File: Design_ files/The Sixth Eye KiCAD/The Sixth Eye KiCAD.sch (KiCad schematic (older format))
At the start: 13 parts, among them J1 Battery conn, J2 US Sensor conn., J3 Vibration out, U1 ATmega328-AU, U2 LTC3525ISC6-5, Y1 8Mhz

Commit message: ploted
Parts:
- added R?: R, symbol Device:R
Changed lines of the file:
@@
 Wire Wire Line
 	4050 4850 4450 4850
+$Comp
+L Device:R R?
+U 1 1 6104FBF0
+P 8700 4950
+F 0 "R?" H 8770 4996 50  0000 L CNN
+F 1 "R" H 8770 4905 50  0000 L CNN
+F 2 "" V 8630 4950 50  0001 C CNN
+F 3 "~" H 8700 4950 50  0001 C CNN
+	1    8700 4950
+	1    0    0    -1
+$EndComp
 $EndSCHEMATC

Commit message: gerbers & drill files
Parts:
- removed R?: R, symbol Device:R
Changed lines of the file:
@@
 Wire Wire Line
 	4050 4850 4450 4850
-$Comp
-L Device:R R?
-U 1 1 6104FBF0
-P 8700 4950
-F 0 "R?" H 8770 4996 50  0000 L CNN
-F 1 "R" H 8770 4905 50  0000 L CNN
-F 2 "" V 8630 4950 50  0001 C CNN
-F 3 "~" H 8700 4950 50  0001 C CNN
-	1    8700 4950
-	1    0    0    -1
-$EndComp
 $EndSCHEMATC

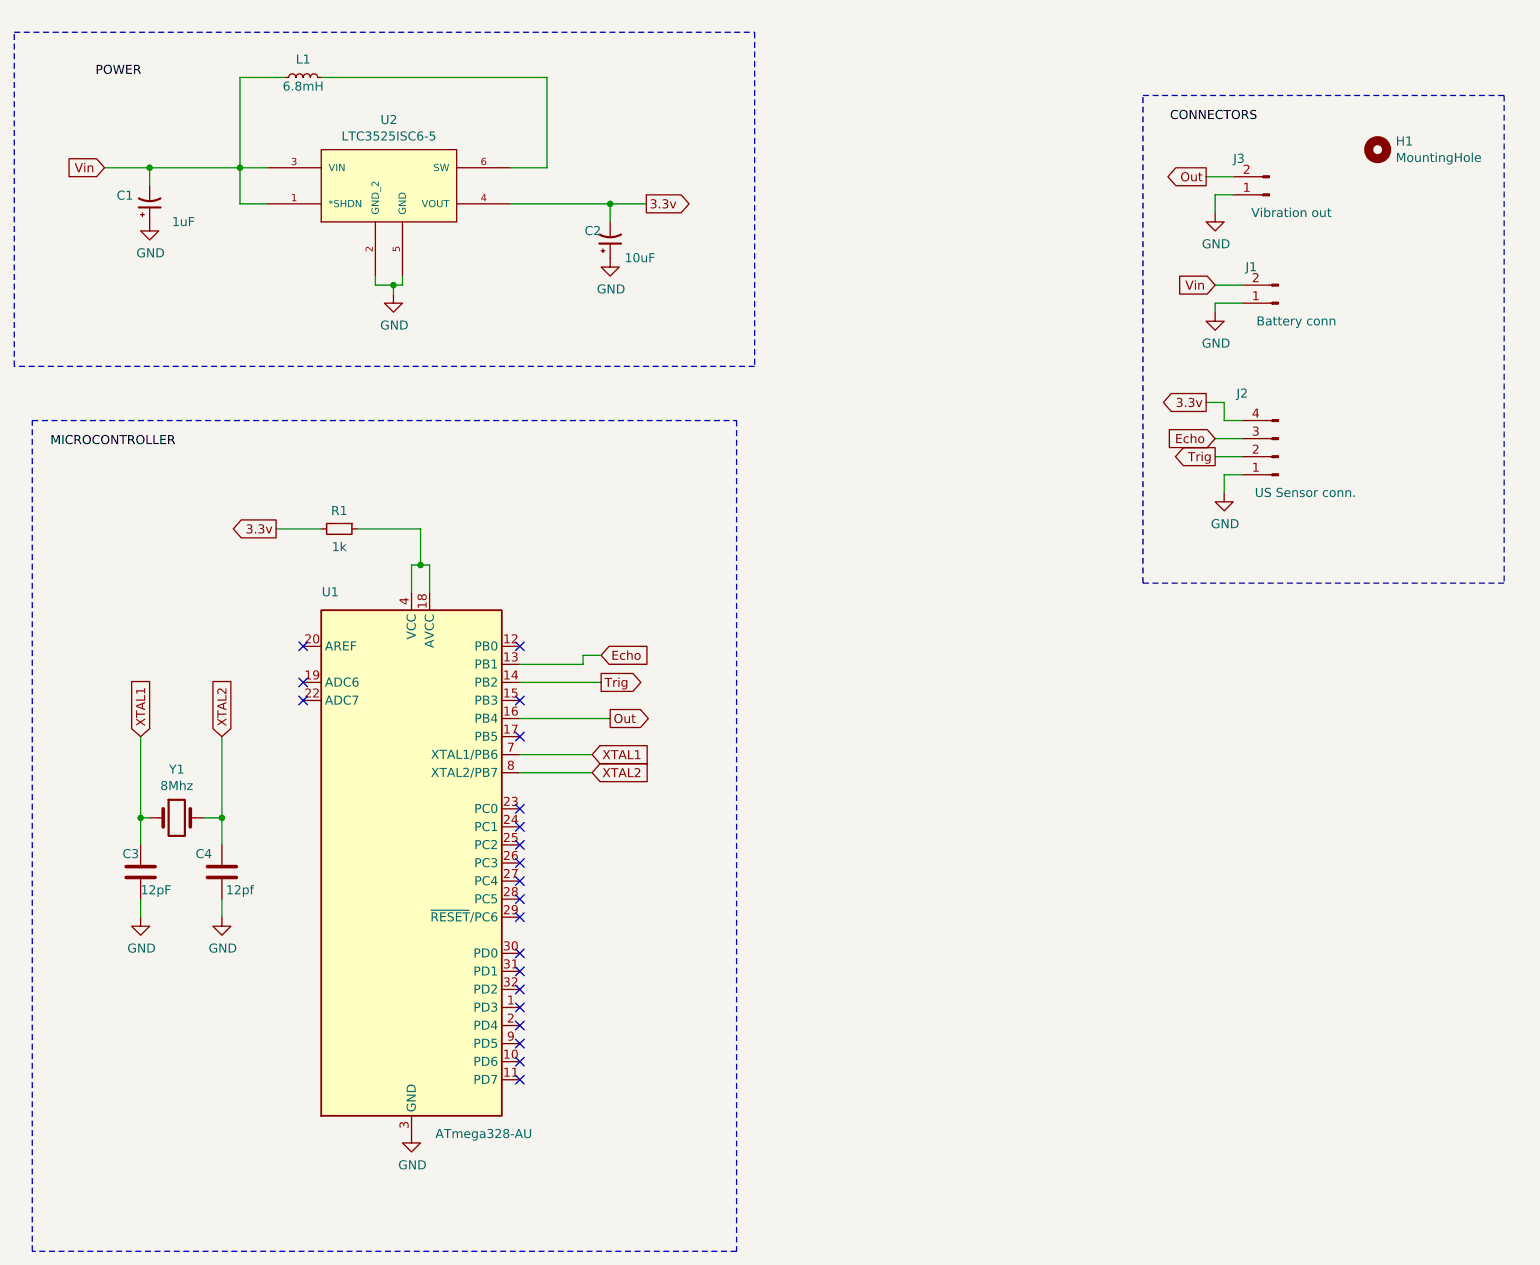
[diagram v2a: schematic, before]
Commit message: Accelerometer added to schematics
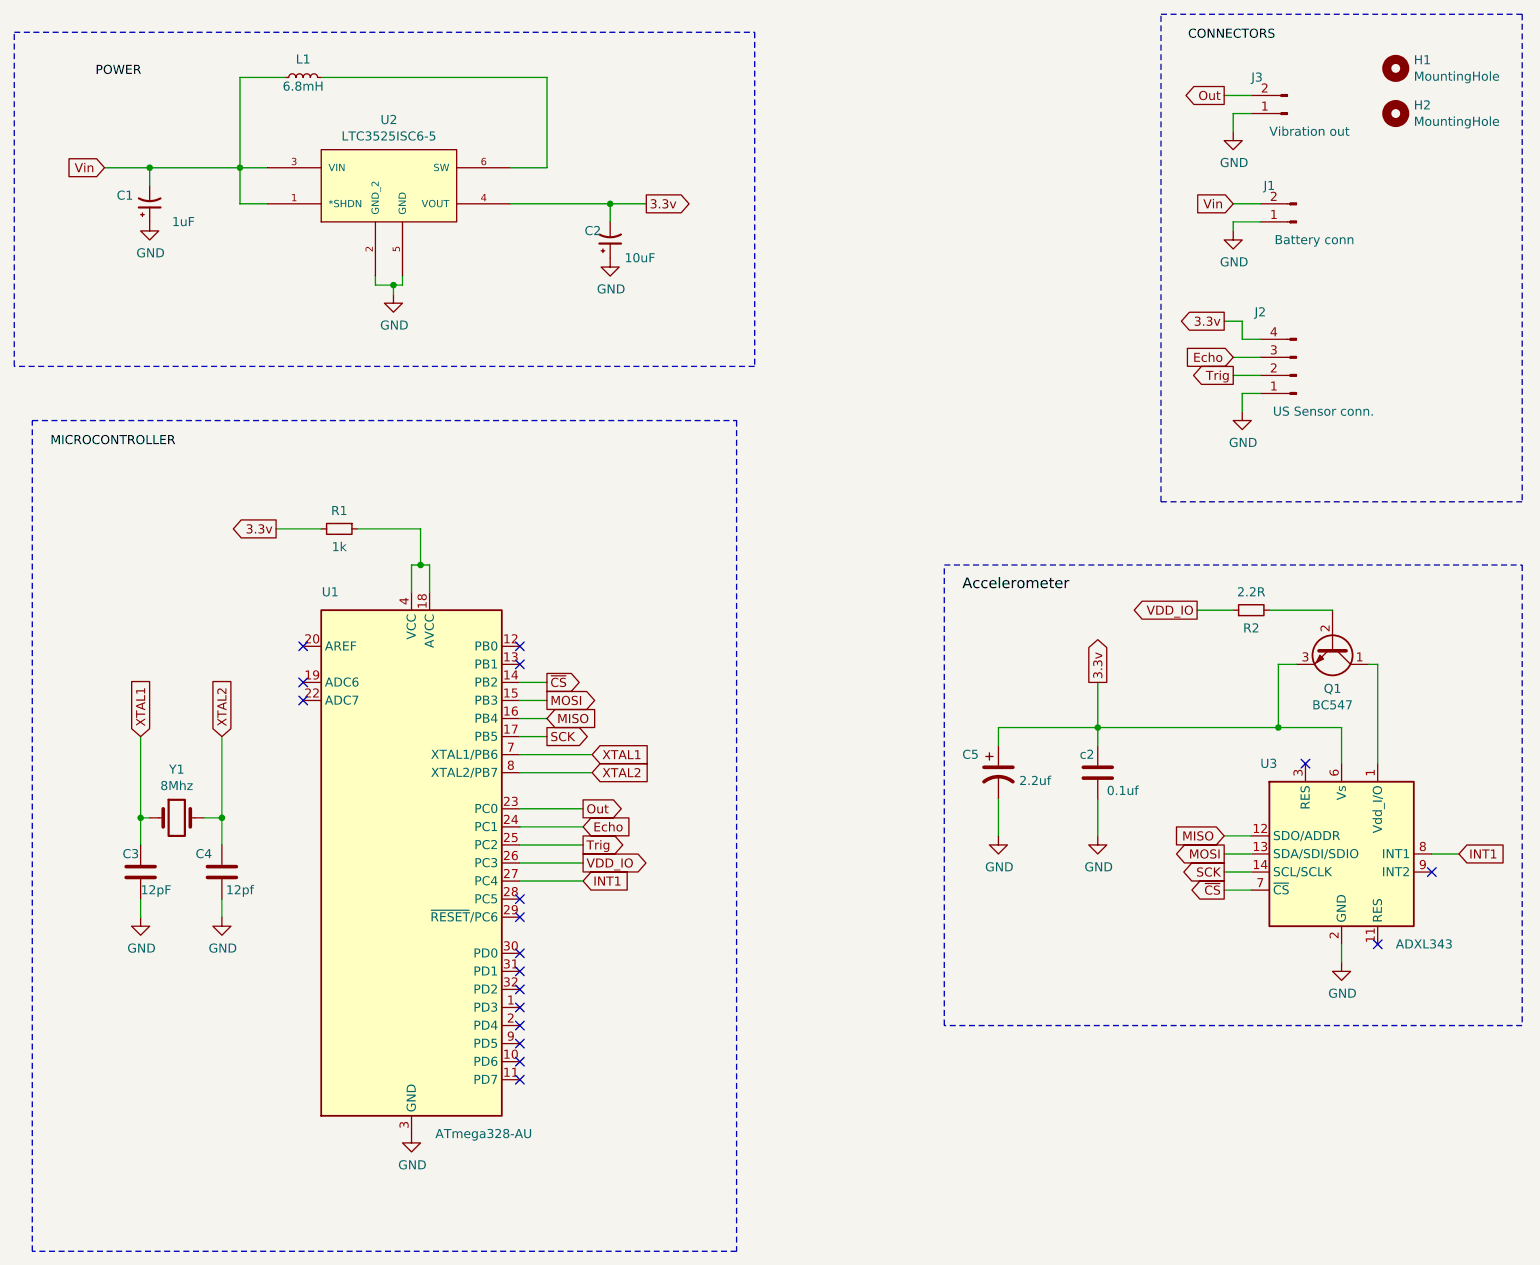
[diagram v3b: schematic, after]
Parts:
- added C5: 2.2uf, symbol Device:CP1
- added H2: MountingHole, MountingHole:MountingHole_2mm, symbol Mechanical:MountingHole
- added Q1: BC547, Package_TO_SOT_THT:TO-92_Inline, symbol Transistor_BJT:BC547
- added R2: 2.2R, symbol Device:R_Small
- added U3: ADXL343, Package_LGA:LGA-14_3x5mm_P0.8mm_LayoutBorder1x6y, symbol Sensor_Motion:ADXL343
- added c2: 0.1uf, symbol Device:C
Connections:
- net 3.3v: now also C5.1, Q1.3 (E), U3.6 (Vs), c2.1
- net Echo: now also U1.24 (PC1); no longer U1.13 (PB1)
- net GND: now also C5.2, U3.2 (GND), U3.4 (GND), U3.5 (GND), c2.2
- net Out: now also U1.23 (PC0); no longer U1.16 (PB4)
- net Trig: now also U1.25 (PC2); no longer U1.14 (PB2)
- net MOSI: now reaches U1.15 (PB3)
- net MOSI: now also U3.13 (SDA/SDI/SDIO)
- net SCK: now reaches U1.17 (PB5)
- net SCK: now also U3.14 (SCL/SCLK)
- net VDD_IO: now reaches U1.26 (PC3)
- net VDD_IO: now also R2.1
- net INT1: now reaches U1.27 (PC4)
- net INT1: now also U3.8 (INT1)
- new net: Q1.1 (C), U3.1 (Vdd_I/O)
- new net: Q1.2 (B), R2.2
- new net MISO: U1.16 (PB4), U3.12 (SDO/ADDR)
- new net ~CS: U1.14 (PB2), U3.7 (~CS)
- no-connect marks 21 -> 18
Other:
- moved on the sheet: H1, J1, J2, J3

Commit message: Accelrometer pcb
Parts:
- removed H1, H2: MountingHole, MountingHole:MountingHole_2mm, symbol Mechanical:MountingHole
- added H1, H2: MountingHole_Pad, MountingHole:MountingHole_2.2mm_M2_DIN965_Pad_TopBottom, symbol Mechanical:MountingHole_Pad
- C5: footprint (none) -> Capacitor_Tantalum_SMD:CP_EIA-1608-10_AVX-L
- C6: renamed from c2; footprint (none) -> Capacitor_Tantalum_SMD:CP_EIA-1608-08_AVX-J
- Q1: footprint Package_TO_SOT_THT:TO-92_Inline -> Package_TO_SOT_SMD:SOT-23
- R2: footprint (none) -> Resistor_SMD:R_0603_1608Metric_Pad0.98x0.95mm_HandSolder
- renumbered J3 to J1, J1 to J2, J2 to J3, U2 to U1, U1 to U2
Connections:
- net GND: now also H1.1, H2.1
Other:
- moved on the sheet: C3, C4, Y1
